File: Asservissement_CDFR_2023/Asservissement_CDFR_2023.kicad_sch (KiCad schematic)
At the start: 126 parts, among them IC1 A3930KJPTR-T, IC2 A3930KJPTR-T, J1 Connecteur batterie, J10 Free Connecteur, J11 Conn_01x02, J12 Conn_01x02, J13 Connecteur Odométrie, J2 Conn_01x03, J3 Conn_01x05, J4 Connecteur Programmation, J5 Conn_01x03, J6 Connecteur Odométrie, J7 Conn_01x03, J8 Conn_01x03, J9 Conn_01x05, Q1 QM6006D, Q10 QM6006D, Q11 QM6006D, Q12 QM6006D, Q13 Q_NMOS_GDS, Q2 QM6006D, Q3 QM6006D, Q4 QM6006D, Q5 QM6006D, Q6 QM6006D, Q7 QM6006D, Q8 QM6006D, Q9 QM6006D, U1 LM317_SOT-223, U3 STM32F401RCTx, U4 LMR16020PDDA, Y1 Crystal_GND24

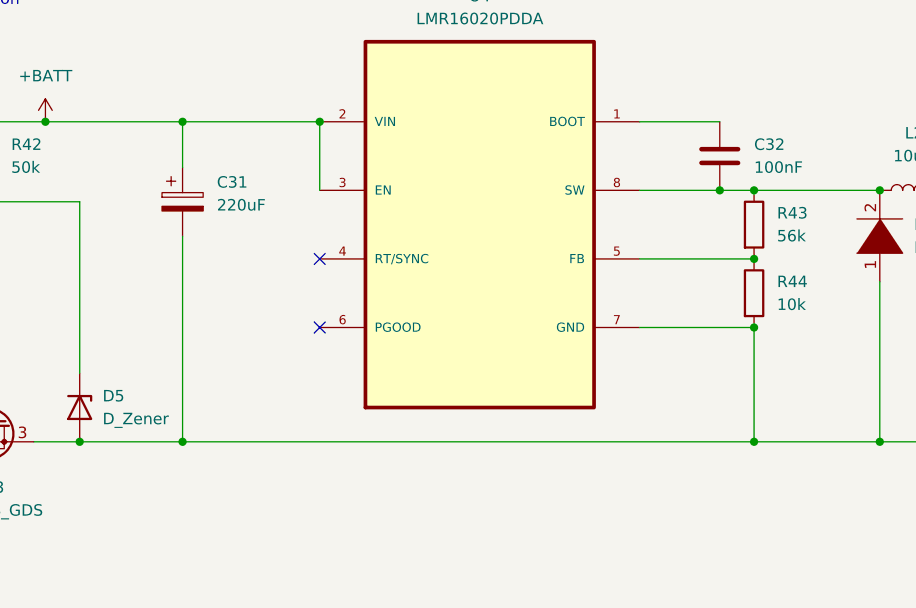
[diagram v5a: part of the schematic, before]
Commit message: New buck routing + caps removal + fix ground on thermal pad for LMR16020 + removal of curved broder
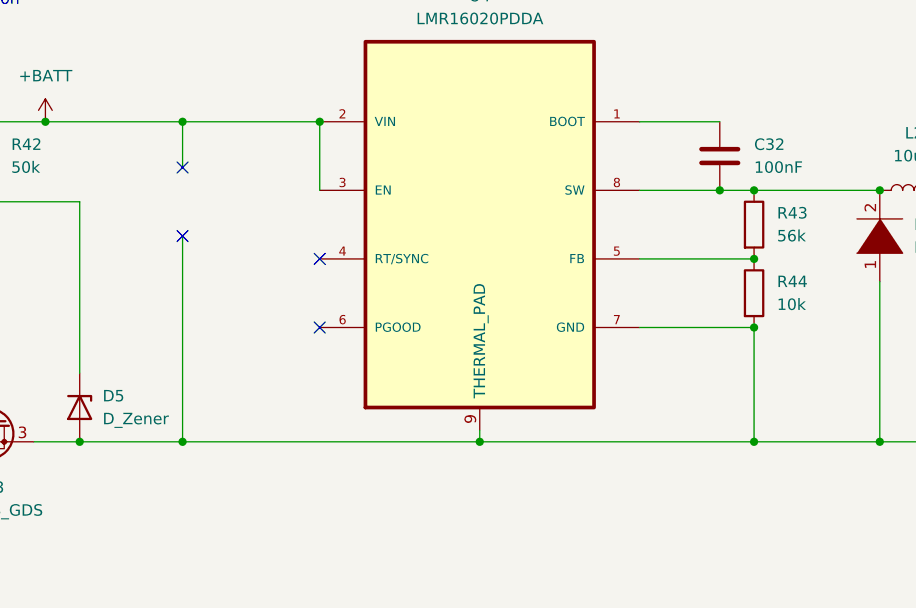
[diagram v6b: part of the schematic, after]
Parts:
- removed C31: 220uF, Capacitor_SMD:CP_Elec_10x10.5, symbol Device:C_Polarized
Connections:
- net GND: now also U4.9 (THERMAL_PAD)
- no-connect marks 19 -> 21
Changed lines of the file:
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@@
   (junction (at 468.63 44.45) (diameter 0) (color 0 0 0 0)
   )
+  (junction (at 101.6 64.77) (diameter 0) (color 0 0 0 0)
+  )
   (junction (at 144.78 278.13) (diameter 0) (color 0 0 0 0)
   )
@@
   (junction (at 250.19 36.83) (diameter 0) (color 0 0 0 0)
   )
+  (no_connect (at 68.58 34.29))
+  (no_connect (at 68.58 41.91))
   (no_connect (at 426.72 241.3))
   (no_connect (at 388.62 266.7))
@@
     (stroke (width 0) (type default) (color 0 0 0 0))
   )
+  (wire (pts (xy 101.6 63.5) (xy 101.6 64.77))
+    (stroke (width 0) (type default) (color 0 0 0 0))
+  )
   (wire (pts (xy 424.18 46.99) (xy 424.18 44.45))
     (stroke (width 0) (type default) (color 0 0 0 0))
@@
     (stroke (width 0) (type default) (color 0 0 0 0))
   )
-  (wire (pts (xy 68.58 64.77) (xy 132.08 64.77))
+  (wire (pts (xy 68.58 64.77) (xy 101.6 64.77))
     (stroke (width 0) (type default) (color 0 0 0 0))
   )
@@
     (stroke (width 0) (type default) (color 0 0 0 0))
   )
+  (wire (pts (xy 101.6 64.77) (xy 132.08 64.77))
+    (stroke (width 0) (type default) (color 0 0 0 0))
+  )
   (wire (pts (xy 128.27 36.83) (xy 132.08 36.83))
     (stroke (width 0) (type default) (color 0 0 0 0))
@@
     (pin "3")
   )
-  (symbol (lib_id "Device:C_Polarized") (at 68.58 38.1 0) (unit 1)
-    (in_bom yes) (on_board yes) (fields_autoplaced)
-    (property "Reference" "C31" (id 0) (at 72.39 35.9409 0)
-      (effects (font (size 1.27 1.27)) (justify left))
-    )
-    (property "Value" "220uF" (id 1) (at 72.39 38.4809 0)
-      (effects (font (size 1.27 1.27)) (justify left))
-    )
-    (property "Footprint" "Capacitor_SMD:CP_Elec_10x10.5" (id 2) (at 69.5452 41.91 0)
-      (effects (font (size 1.27 1.27)) hide)
-    )
-    (property "Datasheet" "~" (id 3) (at 68.58 38.1 0)
-      (effects (font (size 1.27 1.27)) hide)
-    )
-    (pin "1")
-    (pin "2")
-  )
   (symbol (lib_id "Transistor_FET:QM6006D") (at 466.09 102.87 0) (unit 1)
     (in_bom yes) (on_board yes) (fields_autoplaced)
@@
     (pin "7")
     (pin "8")
+    (pin "9")
   )
   (symbol (lib_id "Mechanical:MountingHole_Pad") (at 74.93 391.16 0) (unit 1)
@@
       (reference "C30") (unit 1) (value "100nF") (footprint "Capacitor_SMD:C_0805_2012Metric_Pad1.18x1.45mm_HandSolder")
     )
-    (path "/73b3c49a-d12d-4e39-a41a-5d2e894ec157"
-      (reference "C31") (unit 1) (value "220uF") (footprint "Capacitor_SMD:CP_Elec_10x10.5")
-    )
     (path "/0a8af072-84df-489e-9039-2322dde1fa01"

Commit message: chagement schemas
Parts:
- added C? (x2): 470uF, Capacitor_SMD:CP_Elec_10x10.5, symbol Device:C_Polarized
- C6: value 220uF -> 470uF
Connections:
- net +5V: now also IC1.3 (V5BD_), IC1.4 (V5_), IC2.3 (V5BD_), IC2.4 (V5_), R43.1
- net +BATT: now also C?.1, C?.1
- net GND: now also U4.4 (RT/SYNC), C?.2, C?.2
- net at C32.2, D6.2 (A), L2.1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: no longer R43.1
- no-connect marks 21 -> 14
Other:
- moved on the sheet: C33, D2, D5, D6, L2, Q13, R42, R43, R44, R9

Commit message: chagement composant
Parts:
- C21: value 220uF -> 470uF
- R11, R12, R13, R26, R27, R28: value 52k -> 56k
- R35, R40: value 82k -> 47k
- R36, R41: value 10k -> 15k
- R42: value 50k -> 56k
- gave numbers to parts that had none: 2
